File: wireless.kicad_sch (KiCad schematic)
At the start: 37 parts, among them J1301 U.FL-R-SMT-1, U1301 LBEE5KL1YN-814

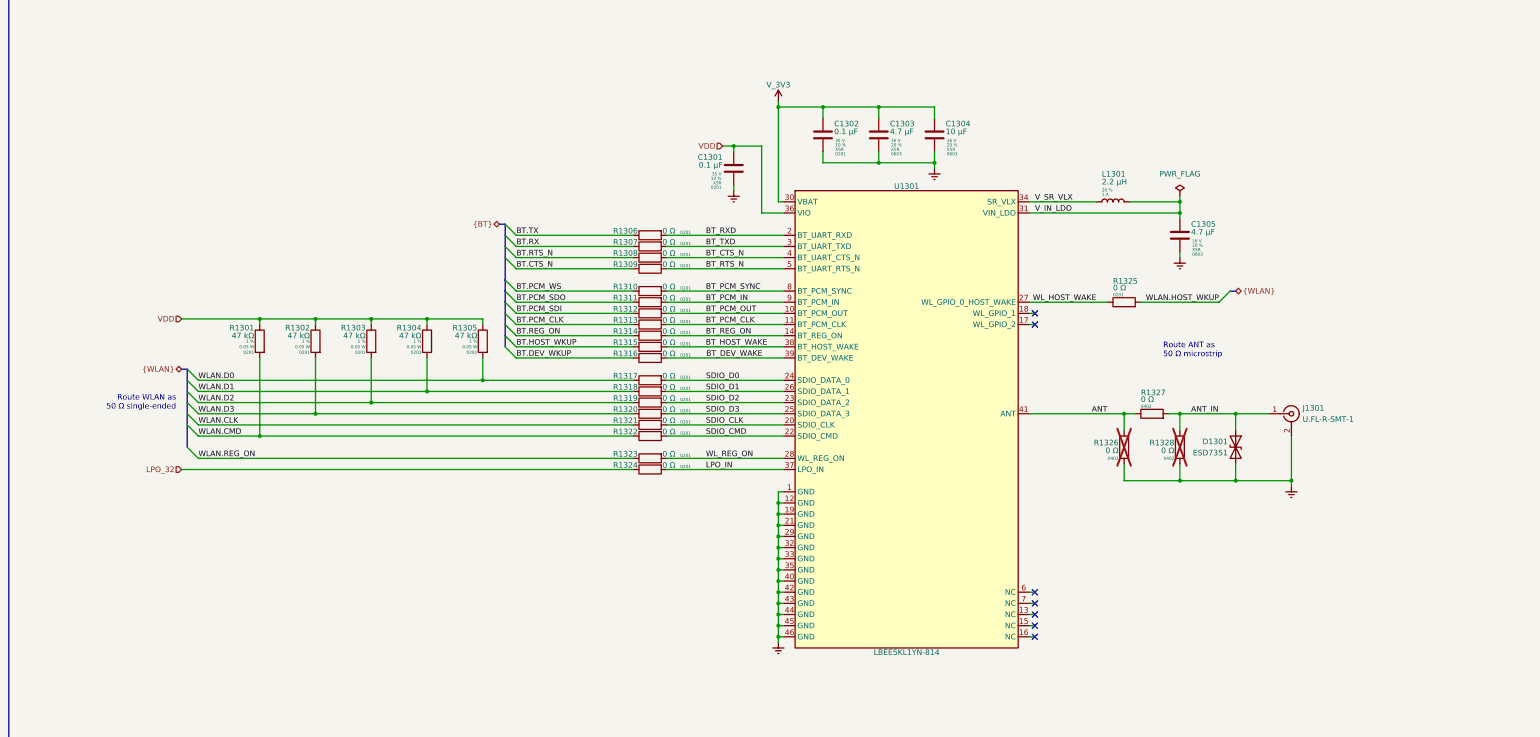
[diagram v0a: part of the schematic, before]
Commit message: Fix power connections
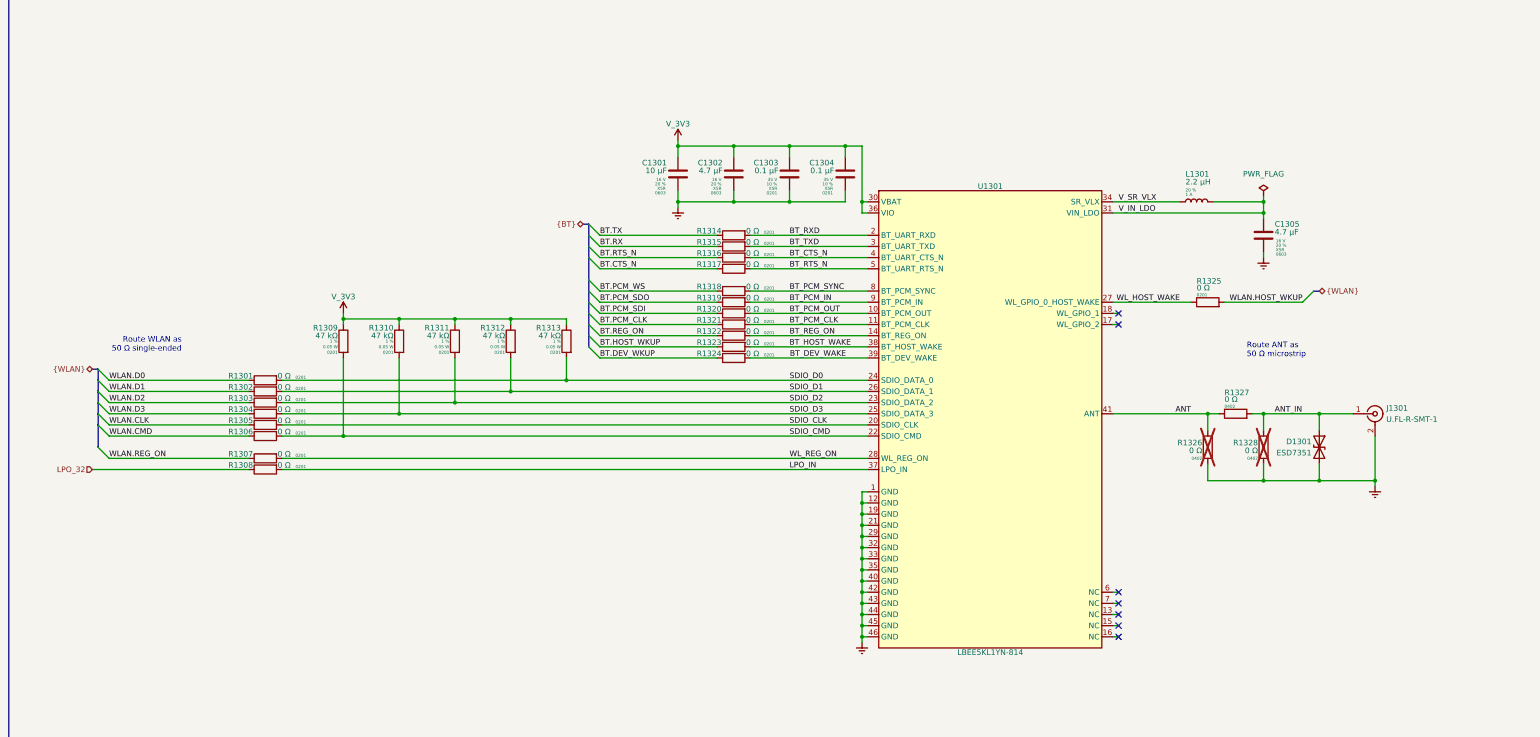
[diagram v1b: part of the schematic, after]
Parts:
- renumbered C1304 to C1301, C1303 to C1302, C1302 to C1303, C1301 to C1304, R1317 to R1301, R1318 to R1302, R1319 to R1303, R1320 to R1304, R1321 to R1305, R1322 to R1306, R1323 to R1307, R1324 to R1308, R1301 to R1309, R1302 to R1310, R1303 to R1311, R1304 to R1312, R1305 to R1313, R1306 to R1314, R1307 to R1315, R1308 to R1316, R1309 to R1317, R1310 to R1318, R1311 to R1319, R1312 to R1320, R1313 to R1321, R1314 to R1322, R1315 to R1323, R1316 to R1324
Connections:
- net VDD is gone; now on net V_3V3: C1304.1, R1309.1, R1310.1, R1311.1, R1312.1, R1313.1, U1301.36 (VIO)
- net SDIO_CMD: now also R1309.2
- net SDIO_D0: now also R1313.2
- net SDIO_D1: now also R1312.2
- net SDIO_D2: now also R1311.2
- net SDIO_D3: now also R1310.2
- net WLAN.CMD: no longer R1309.2
- net WLAN.D0: no longer R1313.2
- net WLAN.D1: no longer R1312.2
- net WLAN.D2: no longer R1311.2
- net WLAN.D3: no longer R1310.2
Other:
- moved on the sheet: C1301, C1302, C1303, C1304, C1305, D1301, J1301, L1301, R1301, R1302, R1303, R1304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

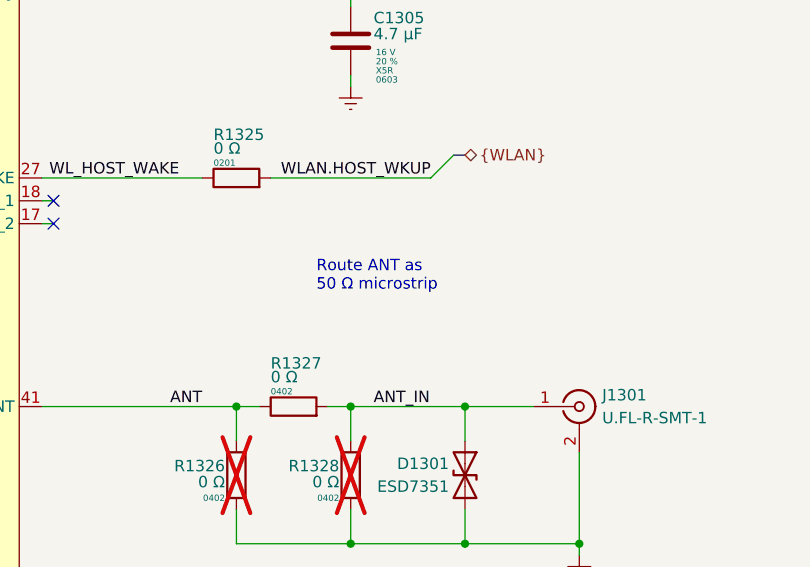
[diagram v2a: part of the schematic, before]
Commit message: Wireless: Route ANT as CPWG
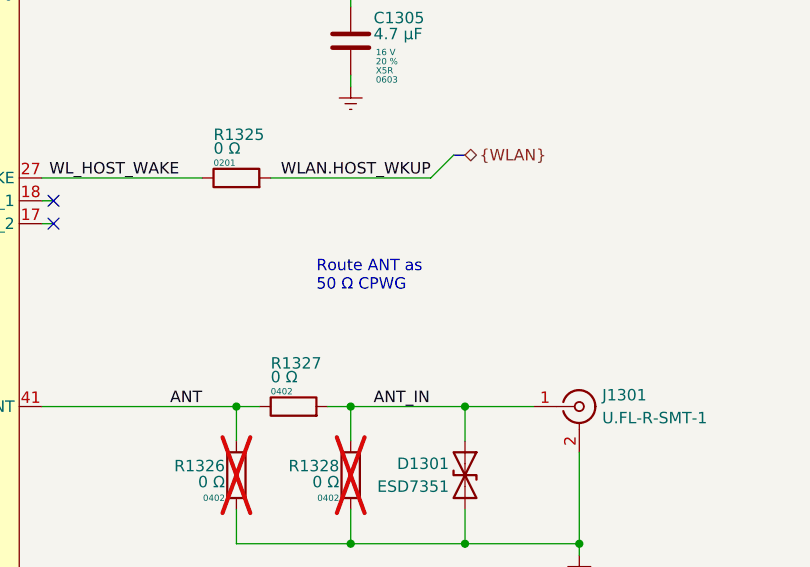
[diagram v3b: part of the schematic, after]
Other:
- note added: "Route ANT as 50 Ω CPWG"
- note removed: "Route ANT as 50 Ω microstrip"
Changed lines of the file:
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@@
 		)
 	)
-	(text "Route ANT as\n50 Ω microstrip"
+	(text "Route ANT as\n50 Ω CPWG"
 		(exclude_from_sim no)
 		(at 294.64 162.56 0)

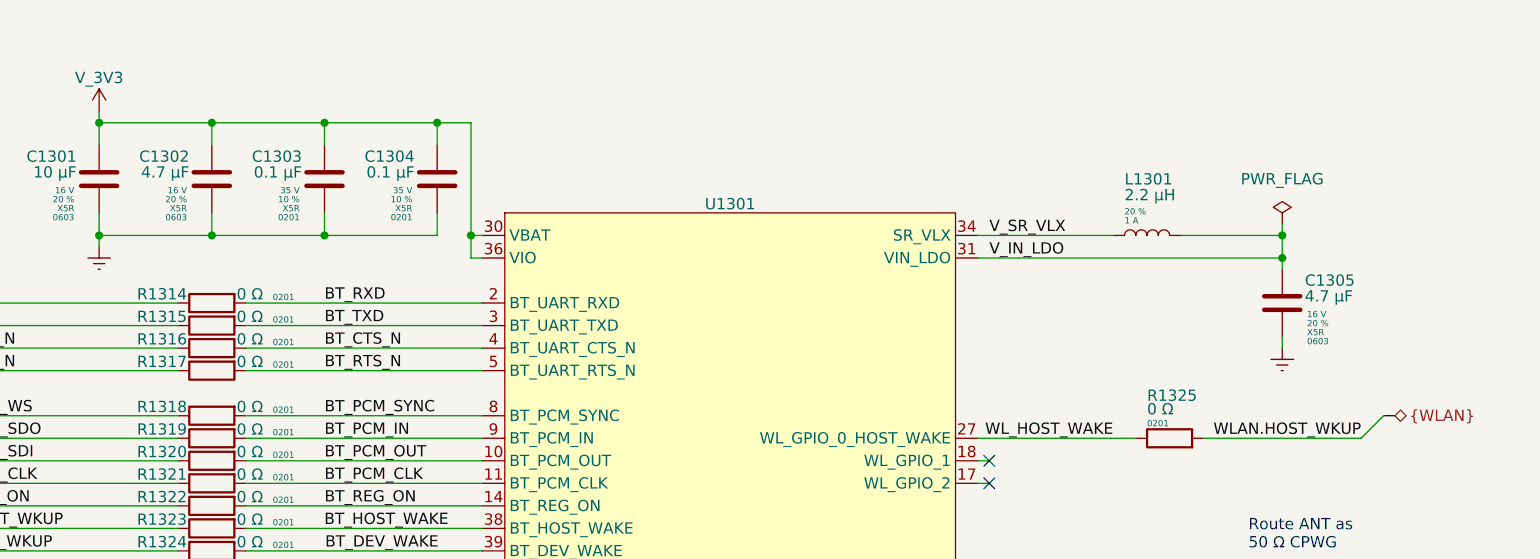
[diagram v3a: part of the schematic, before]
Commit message: Layout the wireless section
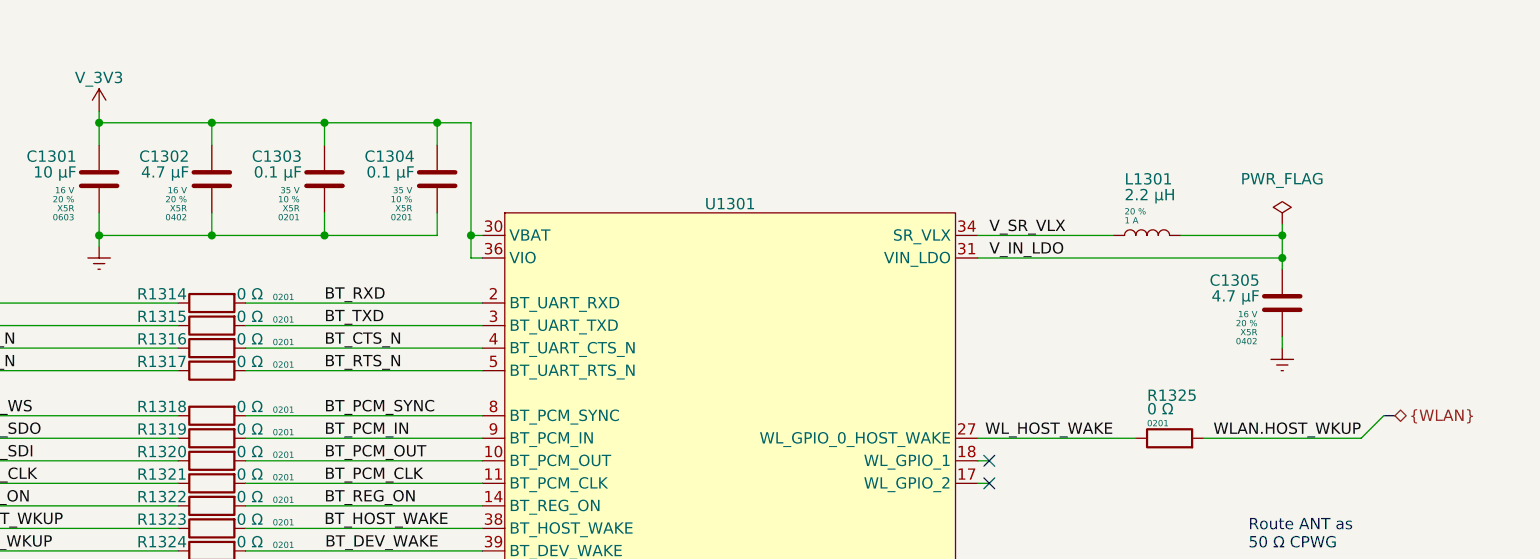
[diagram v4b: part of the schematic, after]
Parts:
- C1302, C1305: footprint Capacitor_SMD:C_0603_1608Metric -> perfect_footprints:C_0402_1005Metric; Digi-Key Part Number 490-7205-1-ND -> 1276-6836-1-ND; MPN GRM188R6YA475KE15D -> CL05A475MO5NUNC; Manufacturer Murata Electronics -> Samsung Electro-Mechanics; Size 0603 -> 0402

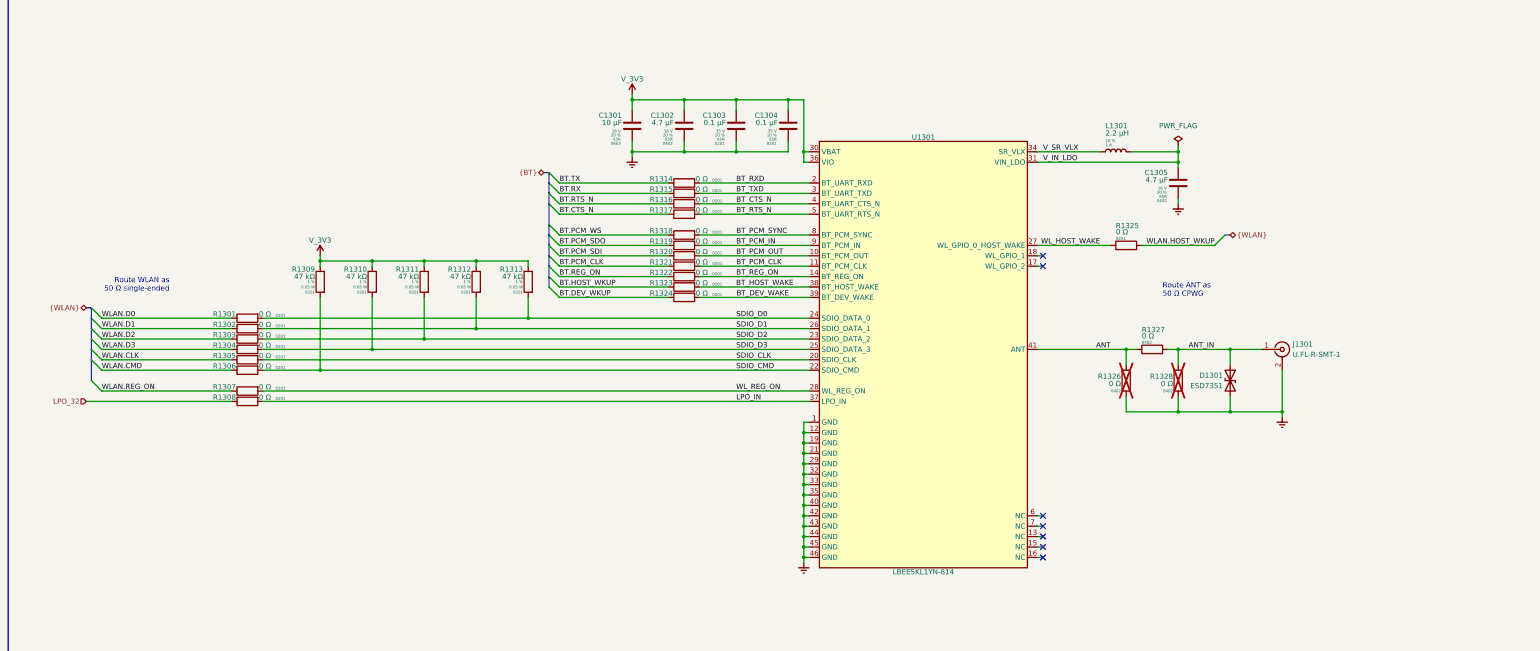
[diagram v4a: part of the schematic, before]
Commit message: Interconnect and length match ETH + Wireless
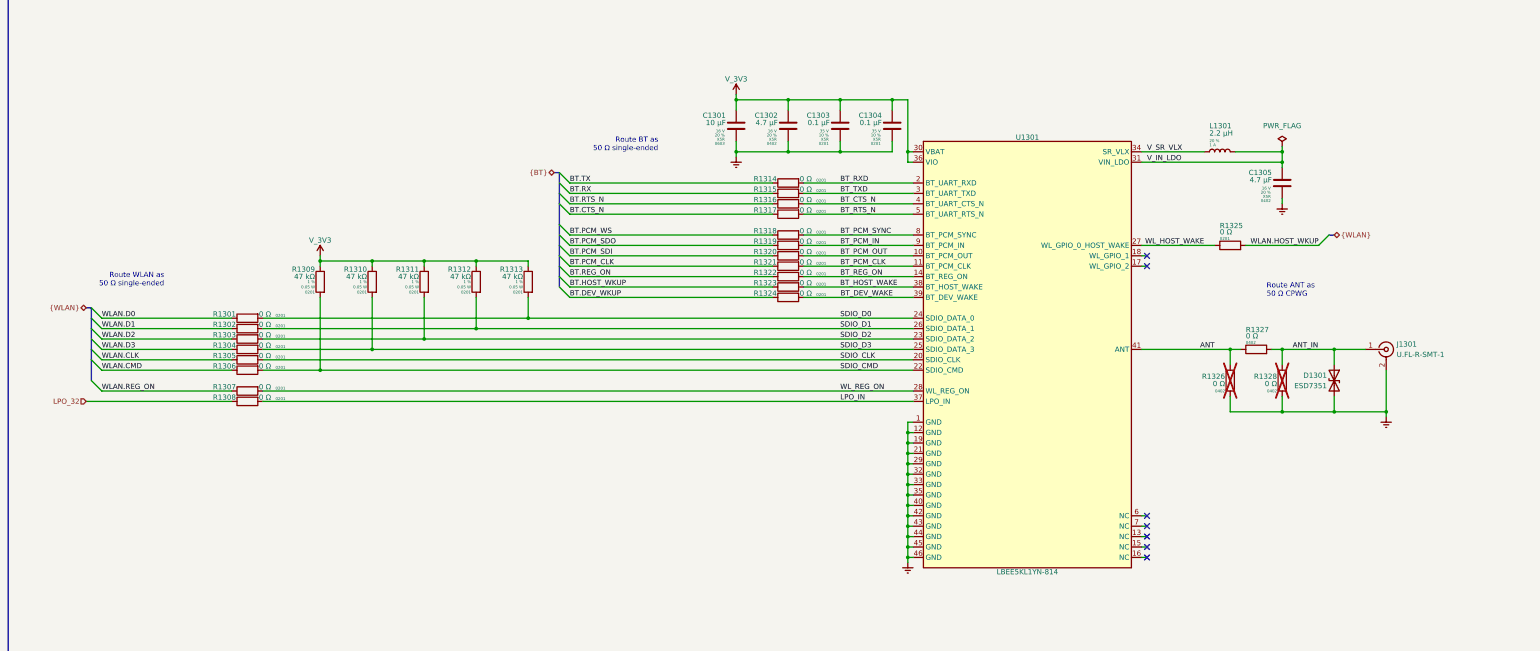
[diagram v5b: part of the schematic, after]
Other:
- note added: "Route BT as 50 Ω single-ended"
- moved on the sheet: C1301, C1302, C1303, C1304, C1305, D1301, J1301, L1301, R1314, R1315, R1316, R1317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

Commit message: Update 0402 footprints
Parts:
- C1302, C1305: footprint perfect_footprints:C_0402_1005Metric -> perfect_footprints:C_0402_1005Metric_HDI
- R1326, R1327, R1328: footprint perfect_footprints:R_0402_1005Metric -> perfect_footprints:R_0402_1005Metric_HDI
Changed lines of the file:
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@@
 			)
 		)
-		(property "Footprint" "perfect_footprints:C_0402_1005Metric"
+		(property "Footprint" "perfect_footprints:C_0402_1005Metric_HDI"
 			(at 322.8848 138.43 0)
 			(effects
@@
 			)
 		)
-		(property "Footprint" "perfect_footprints:R_0402_1005Metric"
+		(property "Footprint" "perfect_footprints:R_0402_1005Metric_HDI"
 			(at 317.5 177.038 90)
 			(effects
@@
 			)
 		)
-		(property "Datasheet" "~"
+		(property "Datasheet" "https://industrial.panasonic.com/ww/products/pt/general-purpose-chip-resistors/models/ERJ2GE0R00X"
 			(at 317.5 175.26 0)
 			(effects
@@
 			)
 		)
-		(property "Description" "Resistor"
+		(property "Description" "0 Ohms Jumper Chip Resistor 0402 (1005 Metric) Automotive AEC-Q200 Thick Film"
 			(at 317.5 175.26 0)
 			(effects
@@
 			)
 		)
-		(property "Datasheet" "~"
+		(property "Datasheet" "https://industrial.panasonic.com/ww/products/pt/general-purpose-chip-resistors/models/ERJ1GN0R00C"
 			(at 311.15 149.86 0)
 			(effects
@@
 			)
 		)
-		(property "Description" "Resistor"
+		(property "Description" "0 Ohms Jumper Chip Resistor 0201 (0603 Metric) Thick Film"
 			(at 311.15 149.86 0)
 			(effects
@@
 			)
 		)
-		(property "Footprint" "perfect_footprints:R_0402_1005Metric"
+		(property "Footprint" "perfect_footprints:R_0402_1005Metric_HDI"
 			(at 325.628 182.88 90)
 			(effects
@@
 			)
 		)
-		(property "Footprint" "perfect_footprints:R_0402_1005Metric"
+		(property "Footprint" "perfect_footprints:R_0402_1005Metric_HDI"
 			(at 312.928 182.88 90)
 			(effects
@@
 			)
 		)
-		(property "Footprint" "perfect_footprints:C_0402_1005Metric"
+		(property "Footprint" "perfect_footprints:C_0402_1005Metric_HDI"
 			(at 202.2348 124.46 0)
 			(effects

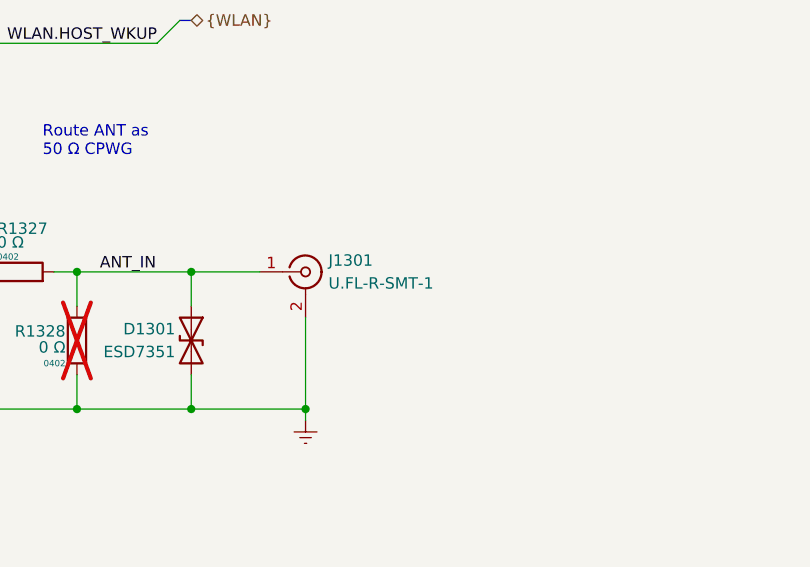
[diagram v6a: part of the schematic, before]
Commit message: Change Wireless antenna connector
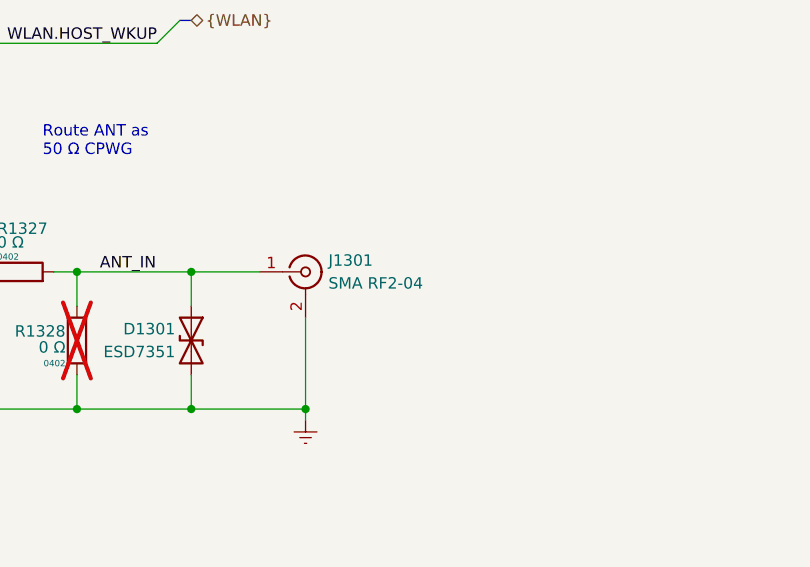
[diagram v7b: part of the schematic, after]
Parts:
- J1301: value U.FL-R-SMT-1 -> SMA RF2-04; footprint Connector_Coaxial:U.FL_Hirose_U.FL-R-SMT-1_Vertical -> Connector_Coaxial:SMA_Amphenol_132134-11_Vertical; Digi-Key Part Number H11891CT-ND -> 2057-RF2-04A-T-00-50-G-ND; MPN U.FL-R-SMT-1(10) -> RF2-04A-T-00-50-G; Manufacturer Hirose Electric Co Ltd -> Adam Tech
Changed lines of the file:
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@@
 			)
 		)
-		(property "Value" "U.FL-R-SMT-1"
+		(property "Value" "SMA RF2-04"
 			(at 351.79 176.53 0)
 			(effects
@@
 			)
 		)
-		(property "Footprint" "Connector_Coaxial:U.FL_Hirose_U.FL-R-SMT-1_Vertical"
+		(property "Footprint" "Connector_Coaxial:SMA_Amphenol_132134-11_Vertical"
 			(at 349.25 175.26 0)
 			(effects
@@
 			)
 		)
-		(property "Datasheet" "https://mm.digikey.com/Volume0/opasdata/d220001/medias/docus/4832/EDC3-302540-10.tif.pdf"
+		(property "Datasheet" "https://app.adam-tech.com/products/download/data_sheet/219105/rf2-04a-t-00-50-g-data-sheet.pdf"
 			(at 349.25 175.26 0)
 			(effects
@@
 			)
 		)
-		(property "Description" "U.FL (UMCC) Connector Receptacle, Male Pin 50 Ohms Surface Mount Solder"
+		(property "Description" "SMA Connector Jack, Female Socket 50 Ohms Through Hole Solder"
 			(at 349.25 175.26 0)
 			(effects
@@
 			)
 		)
-		(property "Digi-Key Part Number" "H11891CT-ND"
+		(property "Digi-Key Part Number" "2057-RF2-04A-T-00-50-G-ND"
 			(at 349.25 175.26 0)
 			(effects
@@
 			)
 		)
-		(property "MPN" "U.FL-R-SMT-1(10)"
+		(property "MPN" "RF2-04A-T-00-50-G"
 			(at 349.25 175.26 0)
 			(effects
@@
 			)
 		)
-		(property "Manufacturer" "Hirose Electric Co Ltd"
+		(property "Manufacturer" "Adam Tech"
 			(at 349.25 175.26 0)
 			(effects
